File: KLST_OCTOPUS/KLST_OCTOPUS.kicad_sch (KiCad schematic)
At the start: 19 parts, among them J1 MIDI IN, J2 MIDI OUT, J3 MIDI THRU, J4 UART, U1 H11L1SR2M, U2 74AHC1G125, U3 74AHC1G125, X1 KLST_ICON

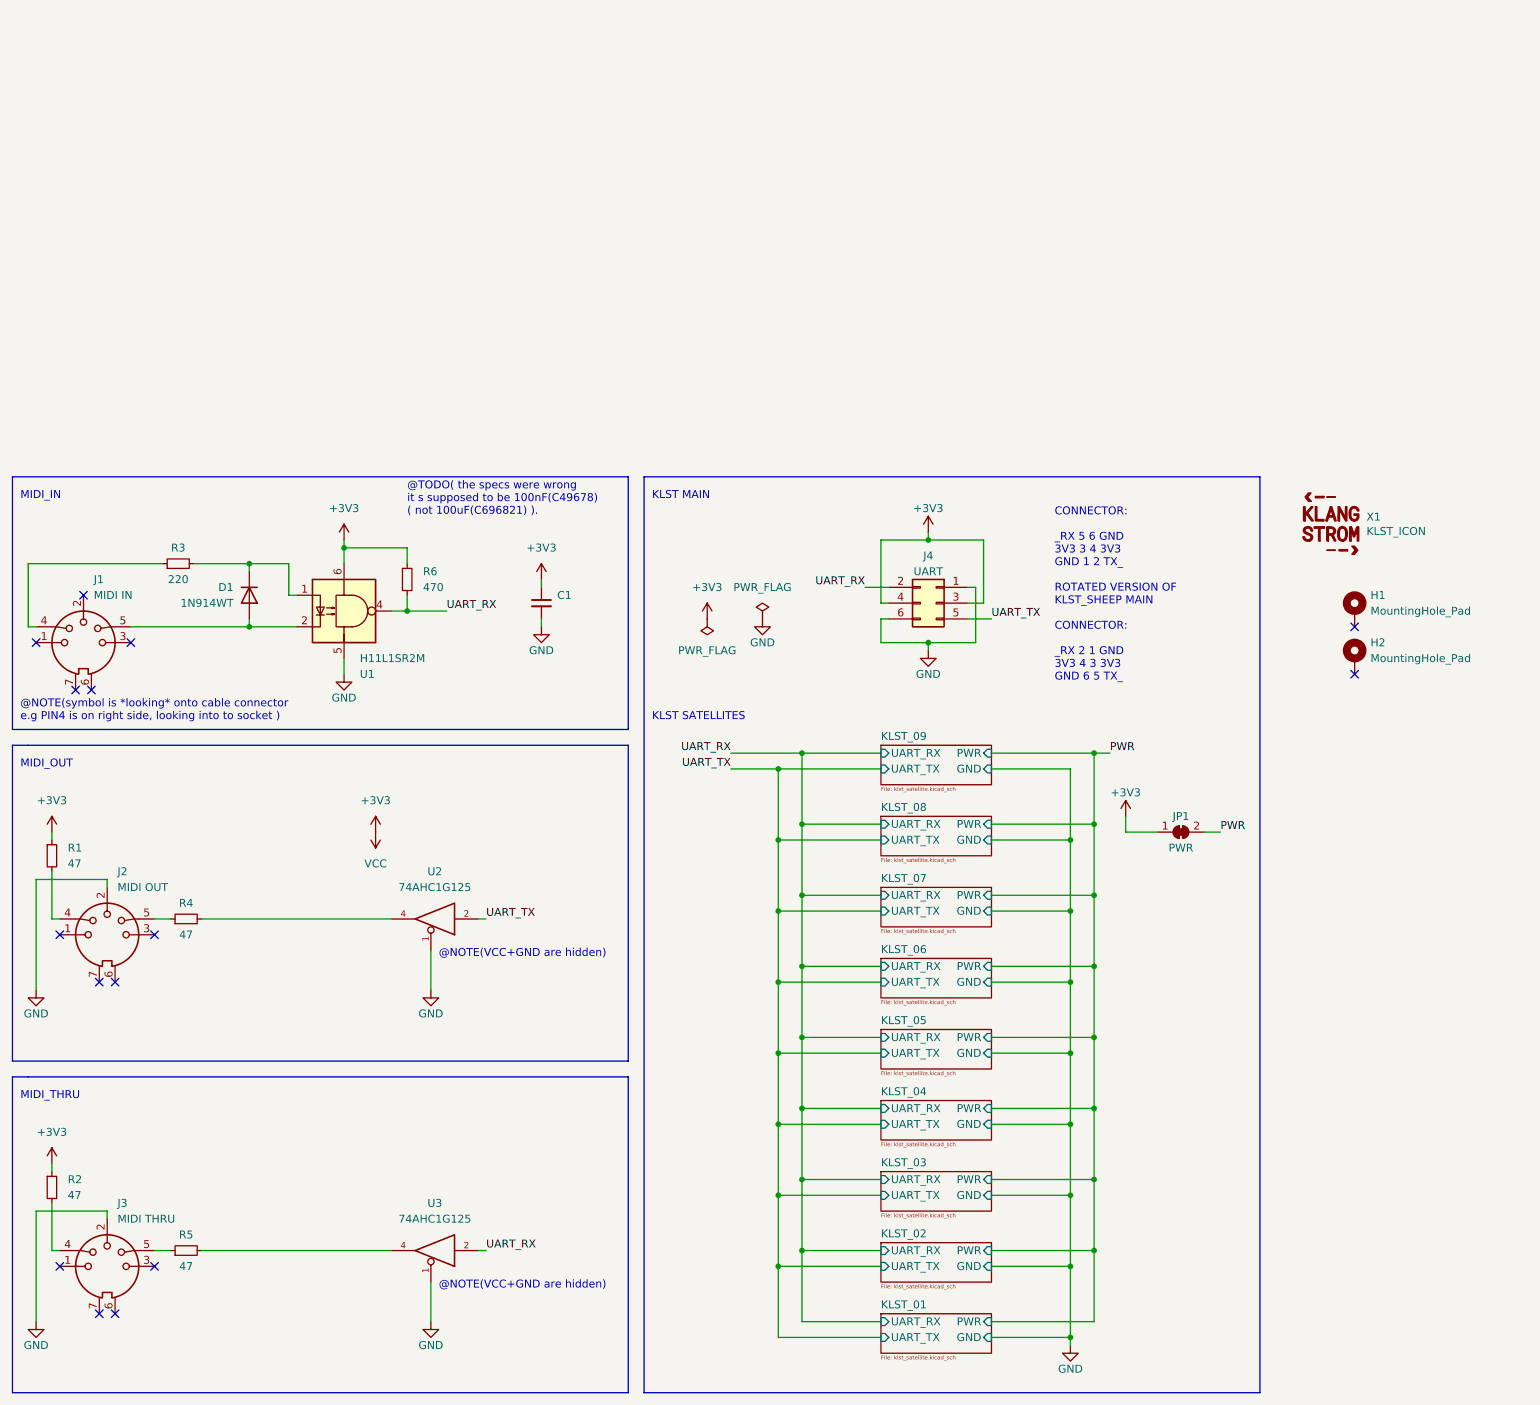
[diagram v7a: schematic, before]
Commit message: fixed bug with TX + buffer
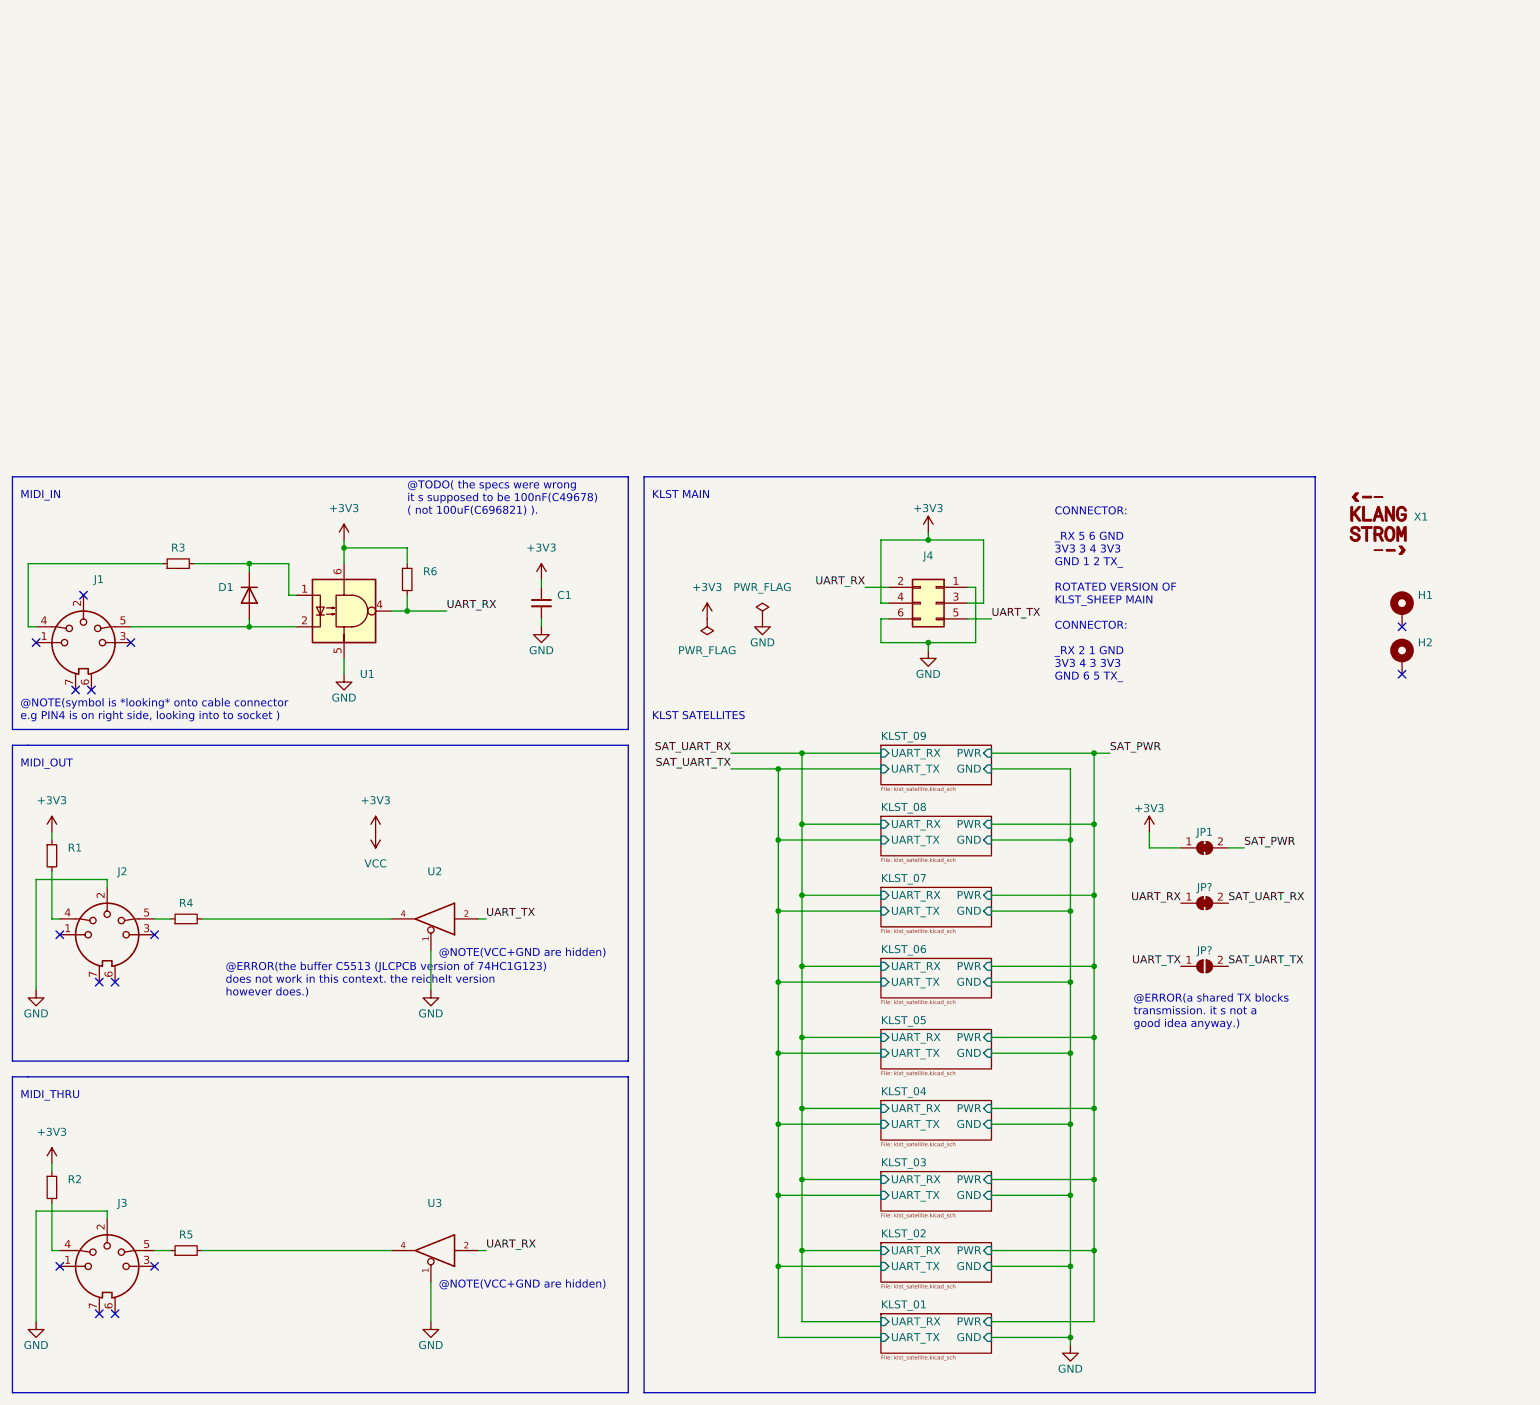
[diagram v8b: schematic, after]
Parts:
- added JP?: (no value), symbol Jumper:SolderJumper_2_Open
- added JP?: (no value), Jumper:SolderJumper-2_P1.3mm_Bridged_RoundedPad1.0x1.5mm, symbol Jumper:SolderJumper_2_Bridged
- D1: value 1N914WT -> (none); footprint Diode_SMD:D_SOD-523 -> (none)
- H1, H2: value MountingHole_Pad -> (none); footprint MountingHole:MountingHole_3.2mm_M3_Pad_Via -> (none)
- J1: value MIDI IN -> (none); footprint DIN-5:DIN5-RA-PTH -> (none)
- J2: value MIDI OUT -> (none); footprint DIN-5:DIN5-RA-PTH -> (none)
- J3: value MIDI THRU -> (none); footprint DIN-5:DIN5-RA-PTH -> (none)
- J4: value UART -> (none); footprint Connector_IDC:IDC-Header_2x03_P2.54mm_Horizontal -> (none)
- JP1: value PWR -> (none); footprint Jumper:SolderJumper-2_P1.3mm_Bridged_RoundedPad1.0x1.5mm -> (none)
- R1, R2, R4, R5: value 47 -> (none); footprint Resistor_SMD:R_0805_2012Metric_Pad1.20x1.40mm_HandSolder -> (none)
- R3: value 220 -> (none); footprint Resistor_SMD:R_0805_2012Metric_Pad1.20x1.40mm_HandSolder -> (none)
- R6: value 470 -> (none); footprint Resistor_SMD:R_0805_2012Metric_Pad1.20x1.40mm_HandSolder -> (none)
- U1: value H11L1SR2M -> (none); footprint Package_DIP:SMDIP-6_W9.53mm -> (none)
- U2, U3: value 74AHC1G125 -> (none); footprint Package_TO_SOT_SMD:SOT-23-5_HandSoldering -> (none)
- X1: value KLST_ICON -> (none); footprint DIN-5:KLST--icon -> (none)
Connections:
- net UART_RX: now also JP?.1 (A)
- net UART_TX: now also JP?.1 (A)
- net PWR renamed SAT_PWR
- new net SAT_UART_RX: JP?.2 (B)
- new net SAT_UART_TX: JP?.2 (B)
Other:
- note added: "@ERROR(a shared TX blocks transmission. it s not a good idea anyway.)"
- note added: "@ERROR(the buffer C5513 (JLCPCB version of 74HC1G123) does not work in this context. the reichelt version however does.)"
- moved on the sheet: H1, H2, JP1
